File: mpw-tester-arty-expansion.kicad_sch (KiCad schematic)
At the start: 111 parts, among them J1 USB4105-GF-A, J10 61300211121, J11 61300211121, J12 61300211121, J14 61300311121, J15 61300311121, J18 61300411121, J19 61300711121, J2 61300211121, J20 61300411121, J3 Arty_A7_SPI, J4 61300211121, J5 61300311121, J6 61300211121, J7 61300211121, J8 61300211121, J9 61300211121, Q1 DTC014TEBTL, U1 SN74LVC1G125DCKR, U2 FT232HQ, U3 SN74LVC1G125DCKR, U4 MAX811REUS+T, U5 NTS0102GT, U6 MCP4661-103E/ML, U7 Caravel_breakout_PCB, U8 W25Q32FVSS, U9 MIC2211-AAYML-TR, Y1 ABM8G-12.000MHZ-18-D2Y-T, Y2 ECS-2520MVLC-100-BN-TR

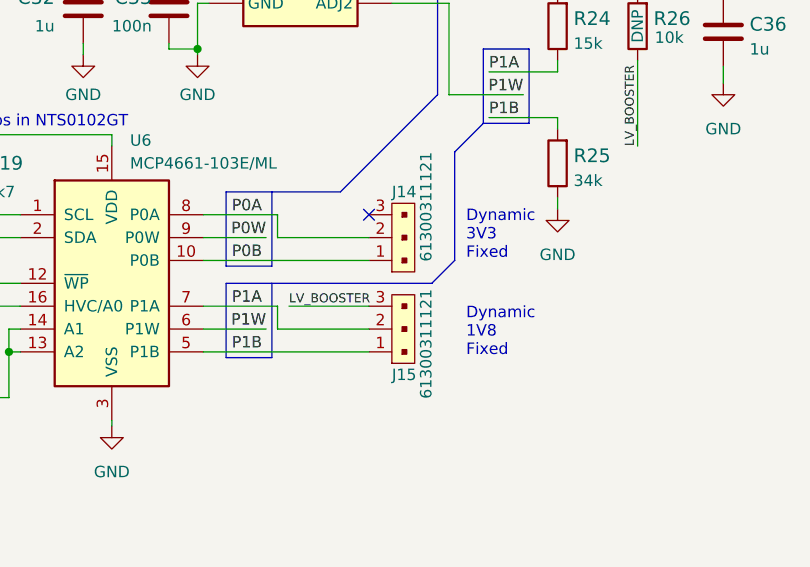
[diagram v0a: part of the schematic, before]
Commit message: Import changes to PCB, adjust placement
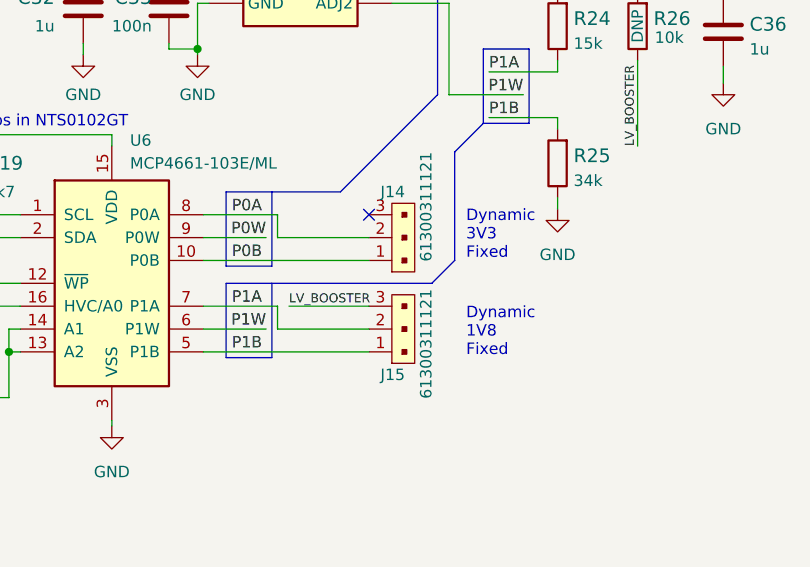
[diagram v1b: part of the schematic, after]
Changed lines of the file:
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@@
   (symbol (lib_id "antmicroRectangularConnectorsHeadersMalePins:61300311121") (at 416.56 112.395 90) (unit 1)
     (in_bom yes) (on_board yes)
-    (property "Reference" "J15" (id 0) (at 415.29 114.935 90)
+    (property "Reference" "J15" (id 0) (at 414.02 114.935 90)
       (effects (font (size 1.27 1.27)) (justify right))
     )
@@
   (symbol (lib_id "antmicroRectangularConnectorsHeadersMalePins:61300311121") (at 416.56 102.235 90) (unit 1)
     (in_bom yes) (on_board yes)
-    (property "Reference" "J14" (id 0) (at 415.29 94.615 90)
-      (effects (font (size 1.27 1.27)) (justify right))
-    )
+    (property "Reference" "J14" (id 0) (at 414.02 94.615 90)
+      (effects (font (size 1.27 1.27)) (justify right))
+    )

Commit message: Change R/C components to 0603 package. Change I2C translator package
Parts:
- removed C1, C10, C11, C13, C14, C15, C16, C18, C19, C20, C21, C22, C23, C24, C25, C26, C27, C28, C29, C30, C31, C33, C34, C5, C7, C8: C_100n_0402, antmicro-footprints:0402-cap, symbol antmicroCapacitors0402:C_100n_0402
- removed C17: C_10n_0402, antmicro-footprints:0402-cap, symbol antmicroCapacitors0402:C_10n_0402
- removed C3, C32, C35, C36, C4: C_1u_0402, antmicro-footprints:0402-cap, symbol antmicroCapacitors0402:C_1u_0402
- removed C6, C9: C_18p_0402, antmicro-footprints:0402-cap, symbol antmicroCapacitors0402:C_18p_0402
- removed R1, R11, R14, R17, R21, R6: R_10k_0402, antmicro-footprints:0402-res, symbol antmicroResistors0402:R_10k_0402
- removed R15, R19: R_4k7_0402, antmicro-footprints:0402-res, symbol antmicroResistors0402:R_4k7_0402
- removed R16, R20: 4x10k_0201_array, antmicro-footprints:EXB18V, symbol antmicroResistorNetworksArrays:4x10k_0201_array
- removed R18: R_0R_0402, antmicro-footprints:0402-res, symbol antmicroResistors0402:R_0R_0402
- removed R2, R3: R_5k1_0402, antmicro-footprints:0402-res, symbol antmicroResistors0402:R_5k1_0402
- removed R7: R_12k_0402, antmicro-footprints:0402-res, symbol antmicroResistors0402:R_12k_0402
- removed R8: 4x0R_0201_array, antmicro-footprints:EXB18V, symbol antmicroResistorNetworksArrays:4x0R_0201_array
- removed U5: NTS0102GT, antmicro-footprints:PSON50P100X195X50-8N, symbol antmicroLogicTranslatorsLevelShifters:NTS0102GT
- added C1, C22, C23, C24, C26, C27, C28, C29, C3, C30, C31, C32, C35, C36: C_1u_0603, antmicro-footprints:0603-cap, symbol antmicroCapacitors0603:C_1u_0603
- added C10, C11, C13, C14, C15, C16, C18, C19, C20, C21, C25, C33, C34, C4, C5, C7, C8: C_100n_0603, antmicro-footprints:0603-cap, symbol antmicroCapacitors0603:C_100n_0603
- added C17: C_10n_0603, antmicro-footprints:0603-cap, symbol antmicroCapacitors0603:C_10n_0603
- added C6, C9: C_18p_0603, antmicro-footprints:0603-cap, symbol antmicroCapacitors0603:C_18p_0603
- added R1, R16, R17, R18, R19, R20, R21, R28, R30, R32, R33, R6: R_10k_0603, antmicro-footprints:0603-res, symbol antmicroResistors0603:R_10k_0603
- added R11, R14, R15, R29, R8: R_0R_0603, antmicro-footprints:0603-res, symbol antmicroResistors0603:R_0R_0603
- added R2, R3: R_5k1_0603, antmicro-footprints:0603-res, symbol antmicroResistors0603:R_5k1_0603
- added R27, R31: R_4k7_0603, antmicro-footprints:0603-res, symbol antmicroResistors0603:R_4k7_0603
- added R7: R_12k_1%_0603, antmicro-footprints:0603-res, symbol antmicroResistors0603:R_12k_1%_0603
- added U?: NTS0102DP, antmicro-footprints:TSSOP-8_W3mm, symbol antmicroLogicTranslatorsLevelShifters:NTS0102DP
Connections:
- net +1V8: now also C36.1
- net +3V3: now also C10.1, C19.1, C20.1, C34.1, C35.1, R1.2, R16.2, R17.1, R18.1, R19.1, R21.1, R28.1, R32.1
- net 3V3_ARTY: now also C1.1, C21.1, U?.3 (VCC_A), U?.6 (OE)
- net 5V0: now also C25.1, C32.1, R20.1, R27.2, R30.1, R31.2, R33.1, U?.7 (VCC_B)
- net 5V0_ARTY: now also C3.1
- net AGND: now also C1.2, C10.2, C11.2, C13.2, C14.2, C15.2, C16.2, C17.2, C18.2, C19.2, C20.2, C21.2, C22.2, C23.2, C24.2, C25.2, C26.2, C27.2, C28.2, C29.2, C3.2, C30.2, C31.2, C32.2, C33.2, C34.2, C35.2, C36.2, C4.2, C5.2, C6.2, C7.2, C8.2, C9.2, R2.2, R29.1, R3.2, R7.1, U?.2 (GND)
- net ARTY_MEM_CS: now also R8.1
- net ARTY_MEM_MISO: now also R15.1
- net ARTY_MEM_MOSI: now also R14.1
- net ARTY_MEM_SCK: now also R11.1
- net ARTY_SCL: now also R31.1, U?.8 (B1)
- net ARTY_SCL_3V3: now also U?.5 (A1)
- net ARTY_SDA: now also R27.1, U?.1 (B2)
- net ARTY_SDA_3V3: now also U?.4 (A2)
- net CC1: now also R2.1
- net CC2: now also R3.1
- net EN_VOUT1: now also R33.2
- net EN_VOUT2: now also R30.2
- net FTDI_3V3: now also C13.1, C15.1, C16.1, C18.1, C4.1, C5.1, C8.1, R6.1
- net FTDI_RESET: now also C17.1, R6.2
- net MEM.SCK: now also R11.2, R18.2
- net MEM.SI: now also R14.2, R19.2
- net MEM.SO: now also R15.2, R21.2
- net MEM.~{CS}: now also R17.2, R8.2
- net MEM.~{HOLD}: now also R32.2
- net MEM.~{WP}: now also R28.2
- net REF: now also R7.2
- net VBUS: now also C7.1
- net VCCA: now also C14.1
- net VCCD: now also C28.1, C31.1
- net VCCD1: now also C24.1
- net VCCD2: now also C22.1
- net VCORE: now also C11.1
- net VDDA: now also C30.1
- net VDDA1: now also C27.1
- net VDDA2: now also C23.1
- net VDDIO: now also C26.1, C29.1
- net XIN: now also C6.1
- net XOUT: now also C9.1
- net ~{UART_EN}: now also R1.1
- net at J4.1, Y2.1 (EN): now also R16.1
- net at U6.12 (~{WP}): now also R20.2
- net at U6.16 (HVC/A0): now also R29.2
- net at U9.4 (BYP): now also C33.1
- no-connect marks 23 -> 21
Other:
- moved on the sheet: J3C

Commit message: Replace remaining 0402 components with 0603 except resistors on USB_D lines
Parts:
- removed C13: C_100n_0603, antmicro-footprints:0603-cap, symbol antmicroCapacitors0603:C_100n_0603
- removed R25: R_34k_0402, antmicro-footprints:0402-res, symbol antmicroResistors0402:R_34k_0402
- added C37: C_100n_0603, antmicro-footprints:0603-cap, symbol antmicroCapacitors0603:C_100n_0603
- added R25: R_34k_0603, antmicro-footprints:0603-res, symbol antmicroResistors0603:R_34k_0603
- added R34: R_10k_0603, antmicro-footprints:0603-res, symbol antmicroResistors0603:R_10k_0603
- gave numbers to parts that had none: 1
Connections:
- net +1V8: now also J12.1; no longer J12.2
- net +3V3: now also J9.1, R34.1; no longer J9.2
- net 5V0: now also C37.1
- net AGND: now also C37.2, R25.1
- net ARTY_XCLK: now also J5.3; no longer J5.1
- net CRVL_~{RST}: now also R34.2
- net P1B: now also R25.2
- net VCCD2: now also J12.2; no longer J12.1
- net VDDA2: now also J9.2; no longer J9.1
- net XCLK_10MHz: now also J5.1; no longer J5.3
- net ~{WP}: now reaches R20.2, U6.12 (~{WP})
- net XCLK_EN: now reaches J4.1, R16.1, Y2.1 (EN)
- net HVC: now reaches R29.2, U6.16 (HVC/A0)
- net BYP: now reaches C33.1, U9.4 (BYP)
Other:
- note added: "Note: internal 10k I2C pullups in NTS0102"
- note removed: "Note: internal pullups in NTS0102GT"
- moved on the sheet: C32, C33, C35, C36, C4, C5, C8, R22, R23, R24, R26, R30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

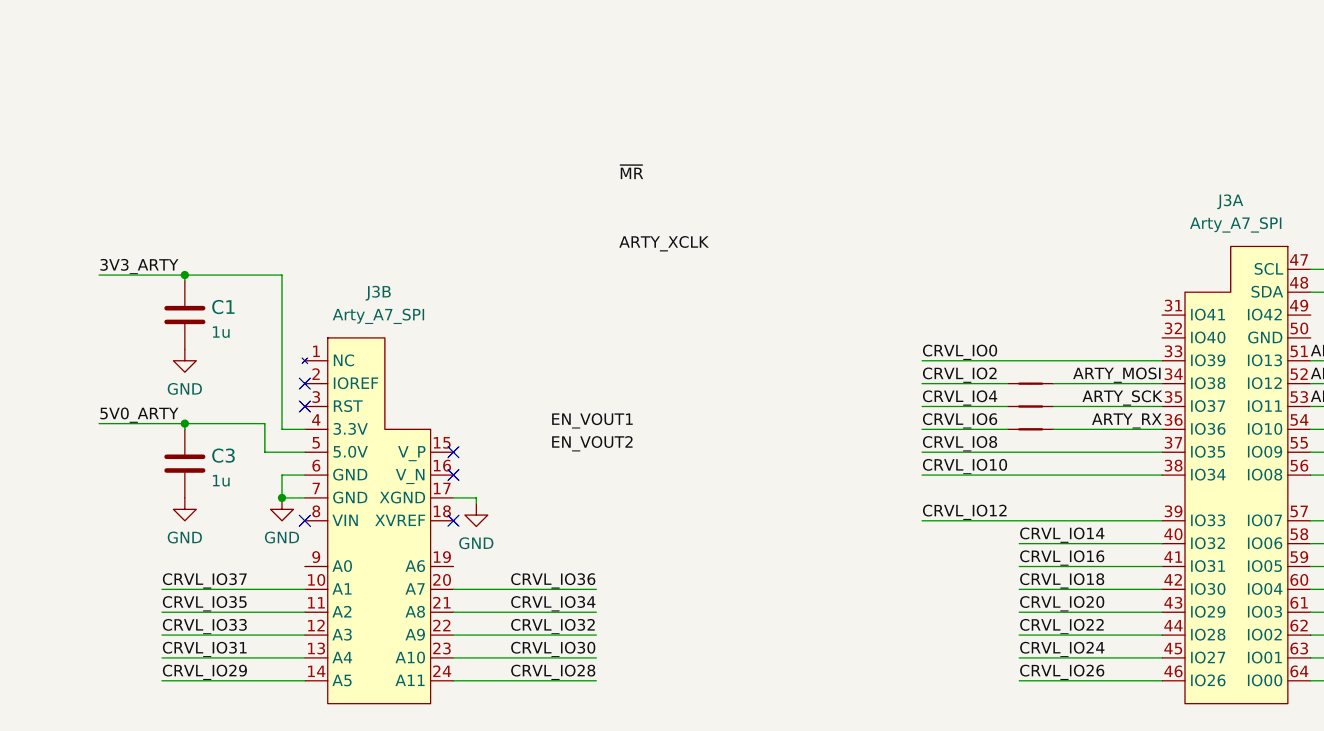
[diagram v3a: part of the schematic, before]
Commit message: Connect remaining singals to Arty
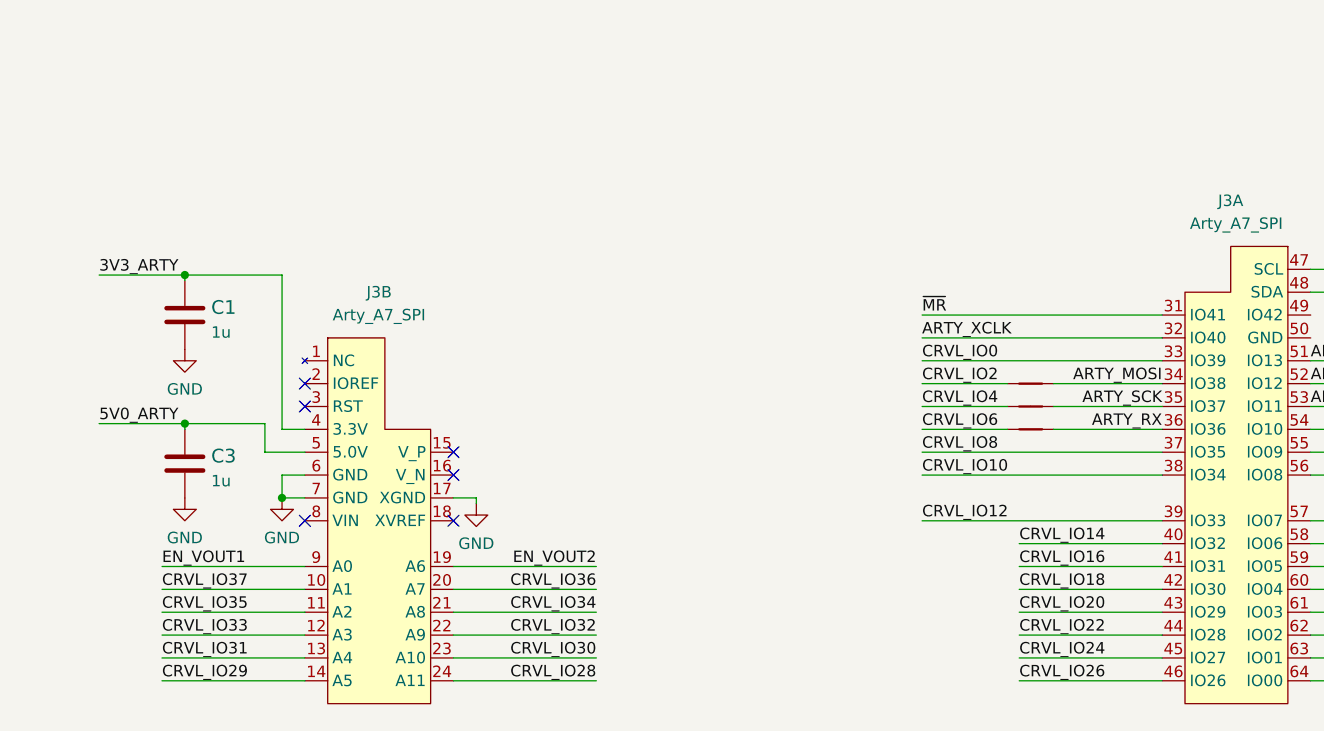
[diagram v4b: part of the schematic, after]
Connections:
- net ARTY_XCLK: now also J3.32 (IO40)
- net EN_VOUT1: now also J3.9 (A0)
- net EN_VOUT2: now also J3.19 (A6)
- net ~{MR}: now also J3.31 (IO41)
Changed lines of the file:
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@@
     (rev "0.0.99")
   )
-  (bus_alias "SPI" (members "~{CS}" "MISO" "MOSI" "SCK"))
   (bus_alias "SPI_FLASH" (members "~{CS}" "SCK" "SI" "SO" "~{WP}" "~{HOLD}"))
+  (bus_alias "SPI" (members "~{CS}" "MISO" "MOSI" "SCK"))
   (junction (at 122.555 74.93) (diameter 0) (color 0 0 0 0)
   )
@@
     (stroke (width 0) (type default) (color 0 0 0 0))
   )
+  (wire (pts (xy 71.12 219.71) (xy 86.995 219.71))
+    (stroke (width 0) (type default) (color 0 0 0 0))
+  )
   (bus (pts (xy 420.37 177.8) (xy 420.37 178.435))
     (stroke (width 0) (type default) (color 0 0 0 0))
@@
     (stroke (width 0) (type default) (color 0 0 0 0))
   )
+  (wire (pts (xy 123.19 194.31) (xy 149.86 194.31))
+    (stroke (width 0) (type default) (color 0 0 0 0))
+  )
   (wire (pts (xy 140.97 126.365) (xy 143.51 126.365))
     (stroke (width 0) (type default) (color 0 0 0 0))
@@
     (stroke (width 0) (type default) (color 0 0 0 0))
   )
+  (wire (pts (xy 38.735 219.71) (xy 54.61 219.71))
+    (stroke (width 0) (type default) (color 0 0 0 0))
+  )
   (wire (pts (xy 307.975 207.645) (xy 316.23 207.645))
     (stroke (width 0) (type default) (color 0 0 0 0))
@@
     (stroke (width 0) (type default) (color 0 0 0 0))
   )
+  (wire (pts (xy 123.19 191.77) (xy 149.86 191.77))
+    (stroke (width 0) (type default) (color 0 0 0 0))
+  )
   (wire (pts (xy 426.085 71.12) (xy 433.705 71.12))
     (stroke (width 0) (type default) (color 0 0 0 0))
@@
     (effects (font (size 1.27 1.27)) (justify right bottom))
   )
-  (label "EN_VOUT1" (at 81.915 204.47 0)
+  (label "EN_VOUT1" (at 38.735 219.71 0)
     (effects (font (size 1.27 1.27)) (justify left bottom))
   )
@@
     (effects (font (size 1.27 1.27)) (justify left bottom))
   )
-  (label "ARTY_XCLK" (at 89.535 184.785 0)
+  (label "ARTY_XCLK" (at 123.19 194.31 0)
     (effects (font (size 1.27 1.27)) (justify left bottom))
   )
@@
     (effects (font (size 1.27 1.27)) (justify left bottom))
   )
-  (label "EN_VOUT2" (at 81.915 207.01 0)
-    (effects (font (size 1.27 1.27)) (justify left bottom))
+  (label "EN_VOUT2" (at 86.995 219.71 180)
+    (effects (font (size 1.27 1.27)) (justify right bottom))
   )
-  (label "~{MR}" (at 89.535 177.165 0)
+  (label "~{MR}" (at 123.19 191.77 0)
     (effects (font (size 1.27 1.27)) (justify left bottom))
   )
